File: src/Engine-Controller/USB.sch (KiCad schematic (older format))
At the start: 1 part, among them J2 USB

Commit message: Resolved all ERC issues
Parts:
- J2: footprint BEL_SS-52300-001 -> Engine-Controller:USB-TypeB
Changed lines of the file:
@@
 $EndDescr
-$Comp
-L Engine-Controller:USB J2
-U 1 1 60FB1D93
-P 5300 4200
-F 0 "J2" H 5193 4767 50  0000 C CNN
-F 1 "USB" H 5193 4676 50  0000 C CNN
-F 2 "BEL_SS-52300-001" H 4950 3600 50  0001 L BNN
-F 3 "" H 5300 4200 50  0001 L BNN
-	1    5300 4200
-	-1   0    0    -1
-$EndComp
 $Comp
 L power:Earth #PWR0110
@@
 Wire Wire Line
 	5700 3900 6200 3900
+$Comp
+L Engine-Controller:USB J2
+U 1 1 61274B9B
+P 5300 4200
+F 0 "J2" H 5193 4767 50  0000 C CNN
+F 1 "USB" H 5193 4676 50  0000 C CNN
+F 2 "Engine-Controller:USB-TypeB" H 4950 3600 50  0001 L BNN
+F 3 "" H 5300 4200 50  0001 L BNN
+	1    5300 4200
+	-1   0    0    -1
+$EndComp
 $EndSCHEMATC

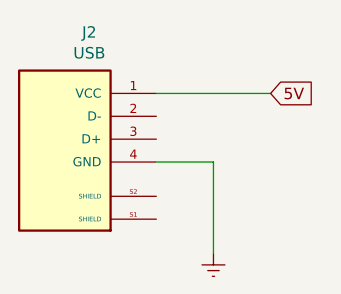
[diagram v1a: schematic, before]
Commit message: Updated Connector pinouts and added button to Reset pin
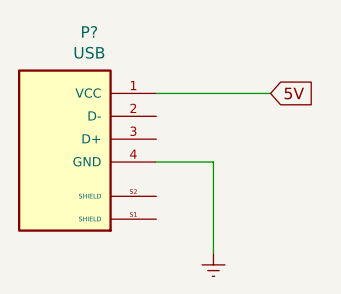
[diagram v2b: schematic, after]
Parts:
- removed J2: USB, Engine-Controller:USB-TypeB, symbol Engine-Controller:USB
- added P?: USB, BEL_SS-52300-001, symbol Engine-Controller:USB
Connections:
- net 5V: now also P?.1 (VCC)
- net Earth: now also P?.4 (GND)
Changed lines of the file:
@@
 	5700 3900 6200 3900
 $Comp
-L Engine-Controller:USB J2
-U 1 1 61274B9B
+L Engine-Controller:USB P?
+U 1 1 60E38DF5
 P 5300 4200
-F 0 "J2" H 5193 4767 50  0000 C CNN
+F 0 "P?" H 5193 4767 50  0000 C CNN
 F 1 "USB" H 5193 4676 50  0000 C CNN
-F 2 "Engine-Controller:USB-TypeB" H 4950 3600 50  0001 L BNN
+F 2 "BEL_SS-52300-001" H 4950 3600 50  0001 L BNN
 F 3 "" H 5300 4200 50  0001 L BNN
 	1    5300 4200

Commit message: Added buffer to some IOs
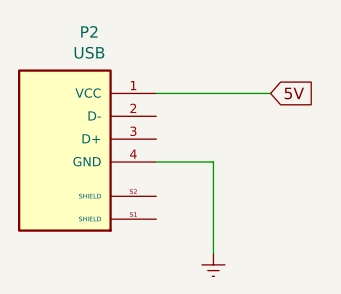
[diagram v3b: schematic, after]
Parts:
- gave numbers to parts that had none: 1
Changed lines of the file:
@@
 	5700 3900 6200 3900
 $Comp
-L Engine-Controller:USB P?
+L Engine-Controller:USB P2
 U 1 1 60E38DF5
 P 5300 4200
-F 0 "P?" H 5193 4767 50  0000 C CNN
+F 0 "P2" H 5193 4767 50  0000 C CNN
 F 1 "USB" H 5193 4676 50  0000 C CNN
 F 2 "BEL_SS-52300-001" H 4950 3600 50  0001 L BNN

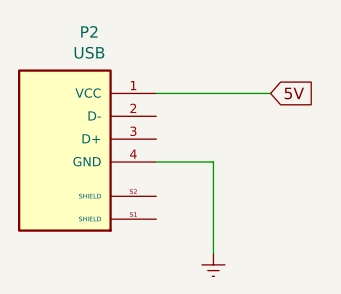
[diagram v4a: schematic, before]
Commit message: Grounded USB shield
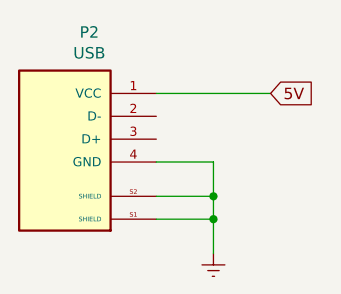
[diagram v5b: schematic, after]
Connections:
- net Earth: now also P2.S1 (SHIELD), P2.S2 (SHIELD)
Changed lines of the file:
@@
 	5700 4200 5950 4200
 Wire Wire Line
-	5950 4200 5950 4600
+	5950 4200 5950 4350
 Text GLabel 6200 3900 2    50   Input ~ 0
 5V
@@
 	-1   0    0    -1
 $EndComp
+Wire Wire Line
+	5700 4350 5950 4350
+Connection ~ 5950 4350
+Wire Wire Line
+	5950 4350 5950 4450
+Wire Wire Line
+	5700 4450 5950 4450
+Connection ~ 5950 4450
+Wire Wire Line
+	5950 4450 5950 4600
 $EndSCHEMATC

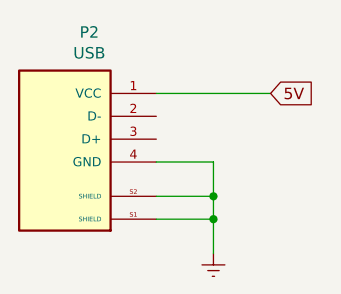
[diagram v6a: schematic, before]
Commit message: Fixed Schematic ERC erros
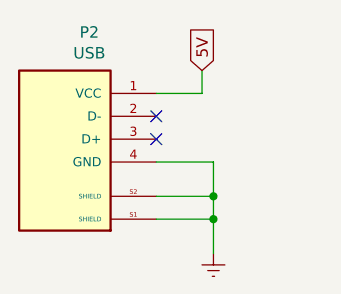
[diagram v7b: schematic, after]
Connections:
- no-connect marks 0 -> 2
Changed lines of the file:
@@
 Wire Wire Line
 	5950 4200 5950 4350
-Text GLabel 6200 3900 2    50   Input ~ 0
-5V
-Wire Wire Line
-	5700 3900 6200 3900
-$Comp
-L Engine-Controller:USB P2
-U 1 1 60E38DF5
-P 5300 4200
-F 0 "P2" H 5193 4767 50  0000 C CNN
-F 1 "USB" H 5193 4676 50  0000 C CNN
-F 2 "BEL_SS-52300-001" H 4950 3600 50  0001 L BNN
-F 3 "" H 5300 4200 50  0001 L BNN
-	1    5300 4200
-	-1   0    0    -1
-$EndComp
 Wire Wire Line
 	5700 4350 5950 4350
@@
 Wire Wire Line
 	5950 4450 5950 4600
+Wire Wire Line
+	5700 3900 5900 3900
+Wire Wire Line
+	5900 3900 5900 3800
+$Comp
+L Engine-Controller:USB P2
+U 1 1 61DDEC99
+P 5300 4200
+F 0 "P2" H 5193 4767 50  0000 C CNN
+F 1 "USB" H 5193 4676 50  0000 C CNN
+F 2 "BEL_SS-52300-001" H 4950 3600 50  0001 L BNN
+F 3 "" H 5300 4200 50  0001 L BNN
+	1    5300 4200
+	-1   0    0    -1
+$EndComp
+Text GLabel 5900 3800 1    50   Input ~ 0
+5V
+NoConn ~ 5700 4000
+NoConn ~ 5700 4100
 $EndSCHEMATC

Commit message: Routed decoupling caps
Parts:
- P2: footprint BEL_SS-52300-001 -> Engine-Controller:USB-TypeB
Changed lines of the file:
@@
 F 0 "P2" H 5193 4767 50  0000 C CNN
 F 1 "USB" H 5193 4676 50  0000 C CNN
-F 2 "BEL_SS-52300-001" H 4950 3600 50  0001 L BNN
+F 2 "Engine-Controller:USB-TypeB" H 4950 3600 50  0001 L BNN
 F 3 "" H 5300 4200 50  0001 L BNN
 	1    5300 4200
